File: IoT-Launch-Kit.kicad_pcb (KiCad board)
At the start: 2 copper layers, 26.4 x 49.9 mm, 21 parts, among them P1 CONN_01X09, P2 CONN_01X09, U1 LD1117S33CTR, U2 CH340G, U3 ESP-12E, U4 USB-A-PLUG, X1 12MHz

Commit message: Fix path references
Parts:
- D1: footprint IoT-Starter-Kit:LED-RGB-5050 -> IoT-Launch-Kit:LED-RGB-5050
- SpaceshipLogo: footprint IoT-Starter-Kit:SpaceshipLogo -> IoT-Launch-Kit:SpaceshipLogo
- U3: footprint IoT-Starter-Kit:ESP-12E -> IoT-Launch-Kit:ESP-12E
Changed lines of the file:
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@@
     )
   )
-  (module IoT-Starter-Kit:ESP-12E (layer F.Cu)
+  (module IoT-Launch-Kit:ESP-12E (layer F.Cu)
     (at 153.67 91.948 270)
     (attr smd)
@@
     )
   )
-  (module IoT-Starter-Kit:LED-RGB-5050 (layer F.Cu)
+  (module IoT-Launch-Kit:LED-RGB-5050 (layer F.Cu)
     (at 153.924 110.998 90)
     (descr "<H3>5050 SMD RGB LED</h3>")
@@
     )
   )
-  (module IoT-Starter-Kit:SpaceshipLogo (layer B.Cu)
+  (module IoT-Launch-Kit:SpaceshipLogo (layer B.Cu)
     (at 153.924 115.062 180)
     (fp_text reference SpaceshipLogo (at 0 13.048124 180) (layer B.SilkS) hide

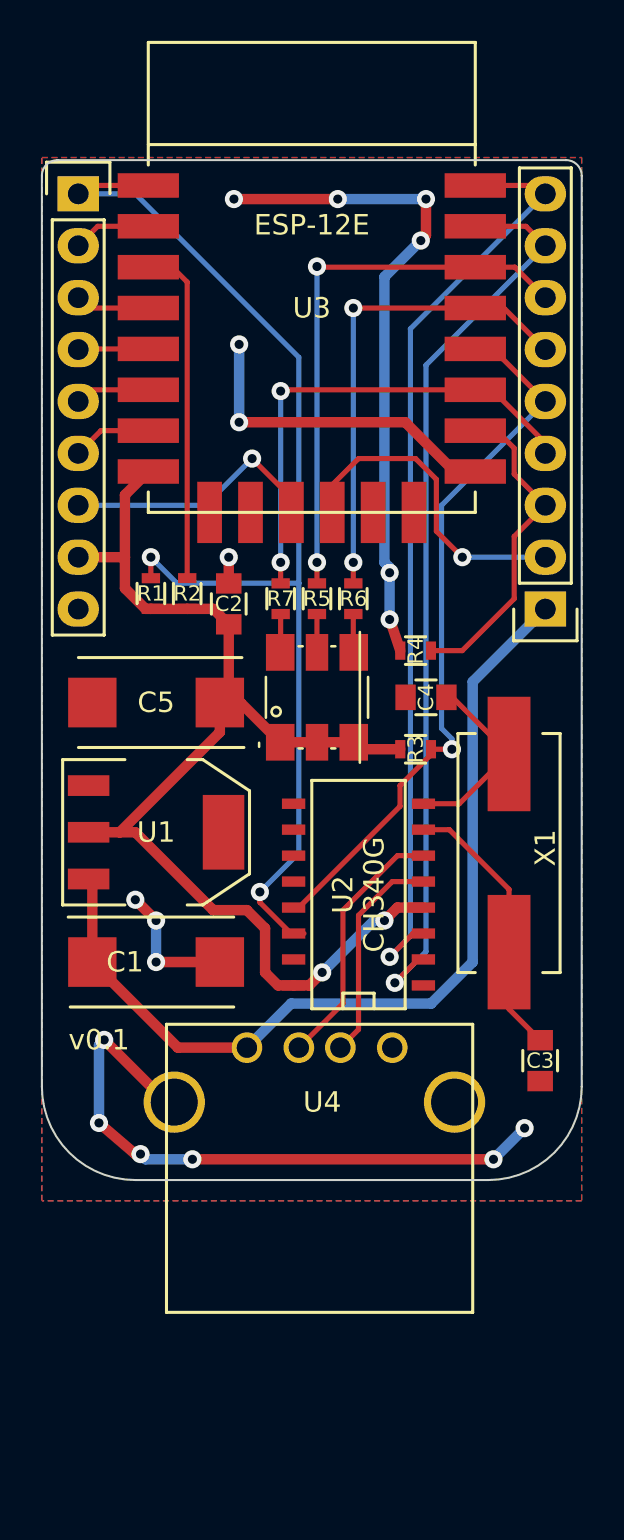
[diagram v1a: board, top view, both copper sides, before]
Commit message: v0.2 of the IoT Launch Kit:  - onboard temperature sensor  - only use the side pins of the ESP12 module  - rearrange pin usage  - slim form factor for fitting into USB slot  - NodeMCU style reset circuit
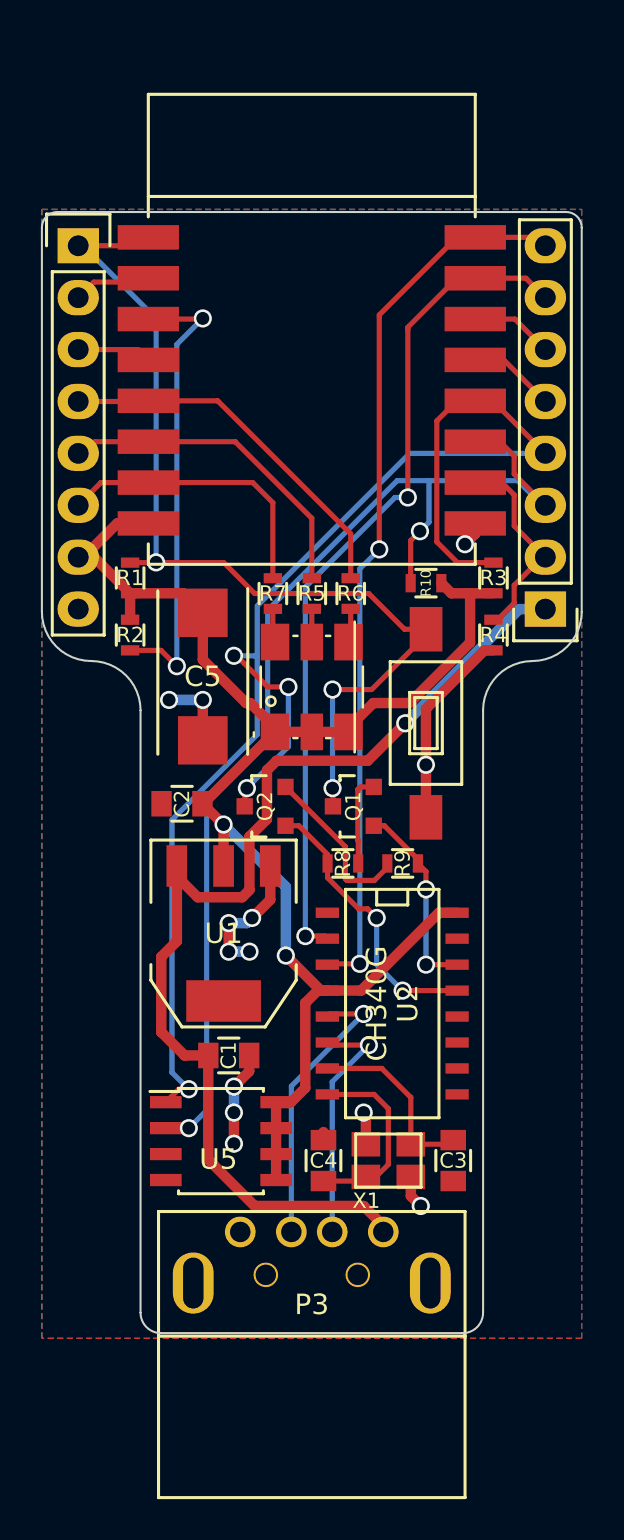
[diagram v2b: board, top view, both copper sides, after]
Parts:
- removed U4: USB-A-PLUG, Connect:USB_A
- added P3: USB_A, IoT-Launch-Kit:USB_A, F.Cu at (153.7, 137.2)
- added Q1: S8050, TO_SOT_Packages_SMD:SOT-23, F.Cu at (155.7, 116.3)
- added Q2: S8050, TO_SOT_Packages_SMD:SOT-23, F.Cu at (151.4, 116.3)
- added R10: 10k, Resistors_SMD:R_0603, F.Cu at (159.3, 105.4)
- added R8: 10k, Resistors_SMD:R_0603, F.Cu at (155.2, 119.1)
- added R9: 10k, Resistors_SMD:R_0603, F.Cu at (158.1, 119.1)
- added SW1: SPST, Buttons_Switches_SMD:SW_SPST_FSMSM, F.Cu at (159.3, 112.3)
- added U5: LM75A, Housings_SOIC:SOIC-8_3.9x4.9mm_Pitch1.27mm, F.Cu at (149.2, 132.7)
- C1: value 100uF -> 10uF; footprint Capacitors_Tantalum_SMD:TantalC_SizeD_EIA-7343_Reflow -> Capacitors_SMD:C_0805
- P1, P2: value CONN_01X09 -> CONN_01X08; footprint Pin_Headers:Pin_Header_Straight_1x09 -> Pin_Headers:Pin_Header_Straight_1x08
- U3: value ESP-12E -> ESP-12; footprint IoT-Launch-Kit:ESP-12E -> IoT-Launch-Kit:ESP-12
- X1: value 12MHz -> CRYSTAL_SMD; footprint Crystals:Crystal_HC49-SD_SMD -> Crystals:crystal_FA238-TSX3225
- moved C4 23.2 mm to (154.2, 133.7), turned to 90 degrees
- moved X1 16.2 mm to (157.4, 133.7), turned to 180 degrees
- moved C2 10.0 mm to (147.3, 116.2), turned to 180 degrees
- moved R3 9.21 mm to (162.6, 105.2), turned to 270 degrees
- moved SpaceshipLogo 6.59 mm to (151.8, 121.3)
- moved C3 6.48 mm to (160.6, 133.7)
- moved U1 5.95 mm to (149.4, 122.6), turned to 180 degrees
- moved C1 5.79 mm to (149.6, 128.5)
- moved U2 5.58 mm to (157.6, 126.0), turned to 270 degrees
- moved R4 3.89 mm to (162.6, 108.0), turned to 90 degrees
- moved R2 3.45 mm to (144.8, 108.0), turned to 90 degrees
- moved C5 2.62 mm to (148.3, 110.0), turned to 270 degrees
- moved P1 2.54 mm to (142.2, 88.9)
- moved U3 2.54 mm to (153.7, 94.5)
- moved R1 1.27 mm to (144.8, 105.2)
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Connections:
- P1 pad 7: GPIO9 -> +3V3
- P1 pad 8: +3V3 -> GND
- P2 pad 2: GPIO10 -> GPIO15
- P2 pad 3: GPIO15 -> GPIO2
- P2 pad 4: GPIO2 -> GPIO0
- P2 pad 5: GPIO0 -> GPIO4
- P2 pad 6: GPIO4 -> GPIO5
- P2 pad 7: GPIO5 -> DIN
- P2 pad 8: DIN -> DOUT
- R5 pad 2: GPIO5 -> GPIO12
- R6 pad 2: GPIO4 -> GPIO14
- R7 pad 2: GPIO2 -> GPIO13
- U2 pad 10: (no net) -> Net-(U2-Pad10)
- U2 pad 11: (no net) -> Net-(U2-Pad11)
- U2 pad 12: (no net) -> Net-(U2-Pad12)
- U2 pad 13: GPIO0 -> DTR
- U2 pad 14: RST -> RTS
- U2 pad 15: (no net) -> Net-(U2-Pad15)
- U2 pad 9: (no net) -> Net-(U2-Pad9)
- U3 pad 10: (no net) -> GPIO15
- U3 pad 11: GPIO9 -> GPIO2
- U3 pad 12: GPIO10 -> GPIO0
- U3 pad 13: (no net) -> GPIO4
- U3 pad 14: (no net) -> GPIO5
- U3 pad 15: GND -> DIN
- U3 pad 16: GPIO15 -> DOUT
- U3 pad 9: (no net) -> GND
- X1 pad 1: Net-(C4-Pad1) -> Net-(C3-Pad1)
- X1 pad 2: Net-(C3-Pad1) -> Net-(C4-Pad1)
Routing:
- net GND: track 87.8 -> 29.6 mm, vias 18 -> 13
- net GPIO0: track 35.5 -> 70.7 mm, vias 1 -> 4
- net GPIO2: track 24.0 -> 55.4 mm
- net GPIO5: track 28.2 -> 4.05 mm, vias 2 -> 0
- net GPIO4: track 24.9 -> 4.27 mm, vias 2 -> 0
- net GPIO10: track 15.8 -> 0.00 mm, vias 1 -> 0
- net GPIO14: track 3.44 -> 18.2 mm
- net +3V3: track 60.2 -> 74.6 mm
- net DTR: track 0.00 -> 14.0 mm, vias 0 -> 2
- net GPIO9: track 12.9 -> 0.00 mm, vias 1 -> 0
- net GPIO12: track 3.67 -> 16.2 mm
- net GPIO13: track 3.89 -> 14.1 mm
- net +5V: track 45.3 -> 55.2 mm, vias 0 -> 1
- net RTS: track 0.00 -> 9.68 mm, vias 0 -> 2
- net RST: track 57.0 -> 48.4 mm, vias 2 -> 3
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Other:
- board size 26.4 x 49.9 mm -> 26.4 x 54.9 mm
- board text added: "GPIO0/SDA"
- board text added: "GPIO4/SCL"
- board text added: "v0.2"
- board text added: "© 2016 Ben Pirt"
- board text removed: "*GPIO10"
- board text removed: "*GPIO9"
- board text removed: "GPIO0"
- board text removed: "v0.1"
- board text removed: "© 2015 Ben Pirt"
